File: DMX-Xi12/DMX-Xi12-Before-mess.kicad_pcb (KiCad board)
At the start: 2 copper layers, 177.8 x 196.8 mm, 190 parts, among them Con1 Cortex-10-SWD, Con10 Screw-terminal, Con11 BARREL_JACK, Con2 Screw-terminal, Con3 Screw-terminal, Con4 Screw-terminal, Con5 Screw-terminal, Con6 Screw-terminal, Con7 Screw-terminal, Con8 Screw-terminal, Con9 Screw-terminal, J1 RJ45, J2 RJ45, P3 USB_B, SW1 Switch_SPDT_x2, SW2 DIPS_04, SW3 SW_PUSH, SW4 SW_PUSH, U1 MAX13450E, U10 BTA20, U11 BTA20, U12 BTA20, U13 BTA20, U14 AN-3003, U15 AN-3003, U16 AN-3003, U17 AN-3003, U18 BTA20, U19 BTA20, U2 LPC11U68JBD100E, U20 BTA20, U21 BTA20, U22 AN-3003, U23 AN-3003, U24 AN-3003, U25 AN-3003, U26 BTA20, U27 BTA20, U28 BTA20, U29 BTA20, U3 LTV-354T*, U30 AN-3003, U31 AN-3003, U32 AN-3003, U33 AN-3003, U34 BTA20, U35 BTA20, U36 BTA20, U37 BTA20, U38 AN-3003, U39 AN-3003, U4 7805n, U40 AN-3003, U41 AN-3003, U42 BTA20, U43 BTA20, U44 BTA20, U45 BTA20, U46 AN-3003, U47 AN-3003, U48 AN-3003, U49 AN-3003, U5 LTV-354T*, U50 BTA20, U51 BTA20, U52 BTA20, U53 BTA20, U54 AN-3003, U55 AN-3003, U56 AN-3003, U57 AN-3003, U58 BTA20, U59 BTA20, U6 AN-3003, U60 BTA20, U61 BTA20, U62 AN-3003, U63 AN-3003, U64 AN-3003, U65 AN-3003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

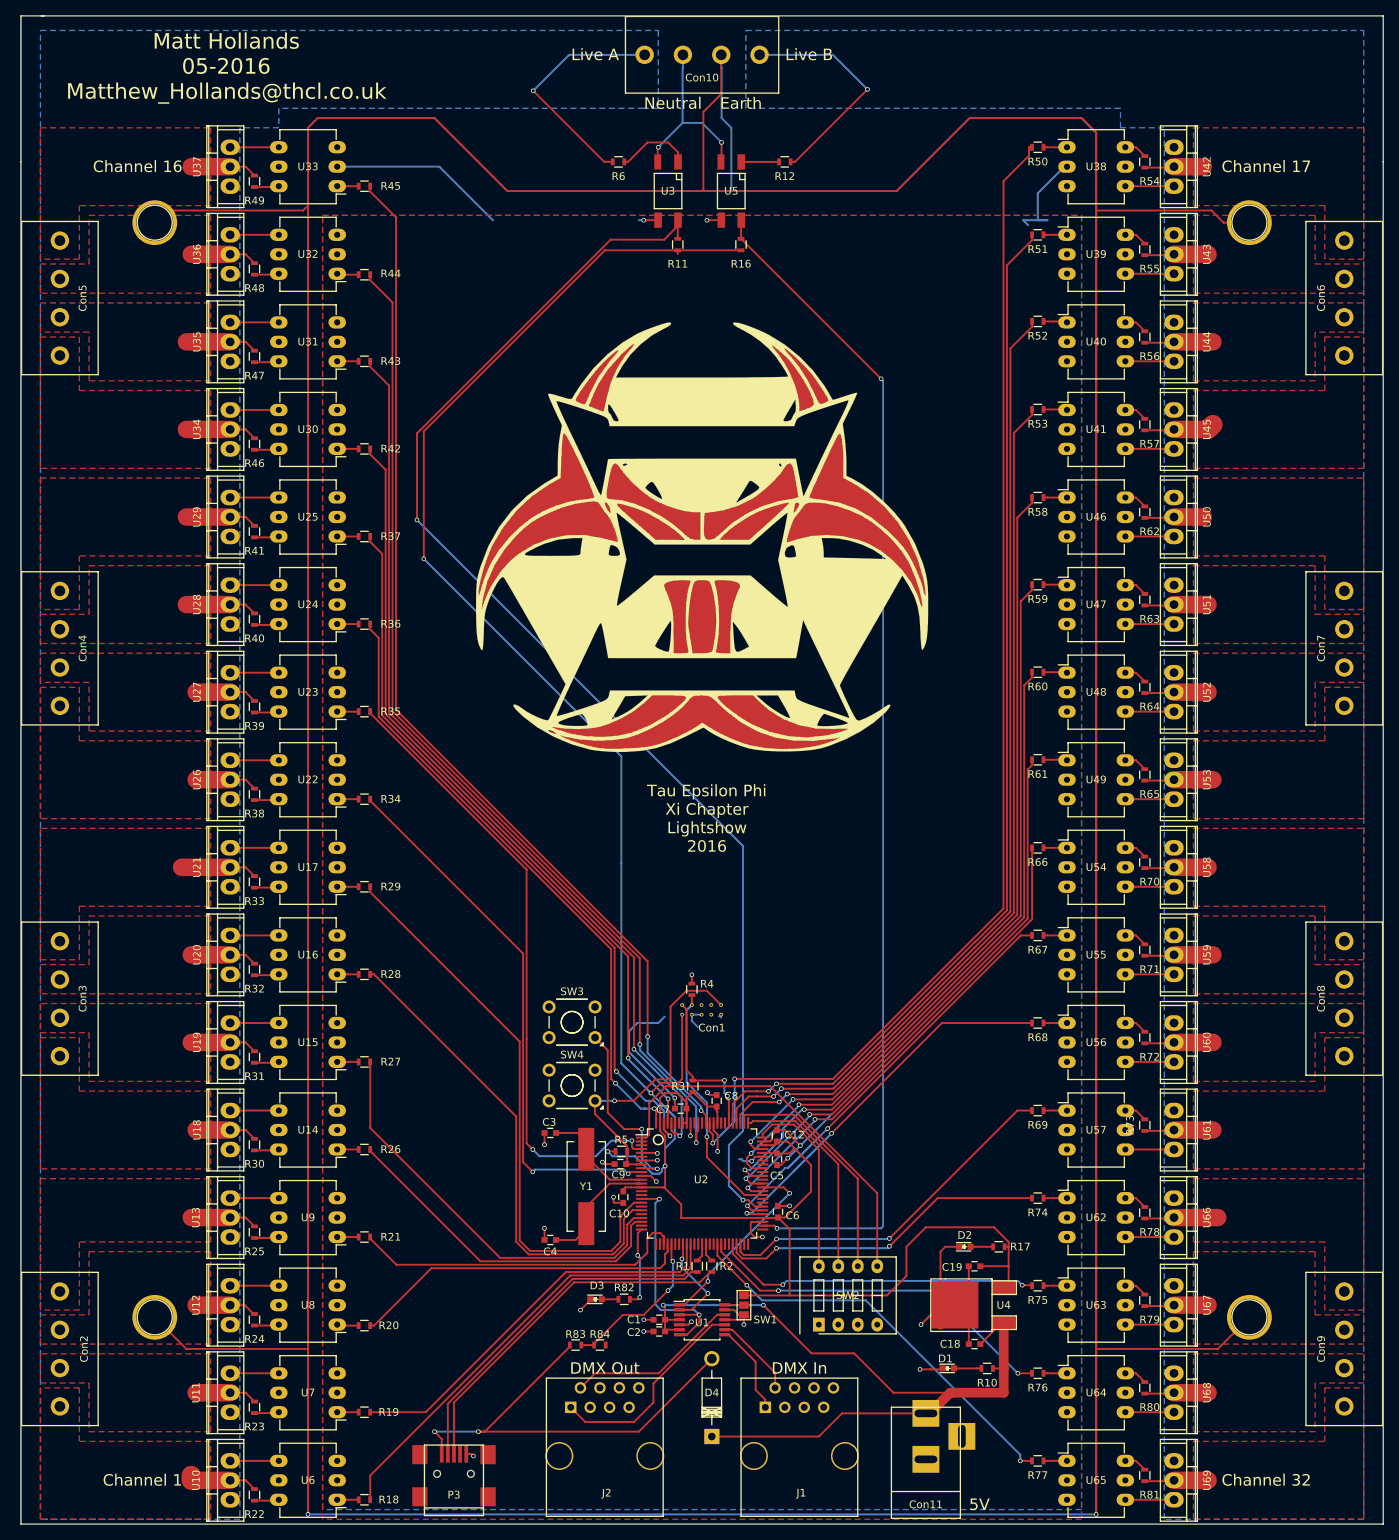
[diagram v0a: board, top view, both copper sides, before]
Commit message: completed board. Schematic, is correct but some part values and numbers need updating! Do not trust the schematic yet
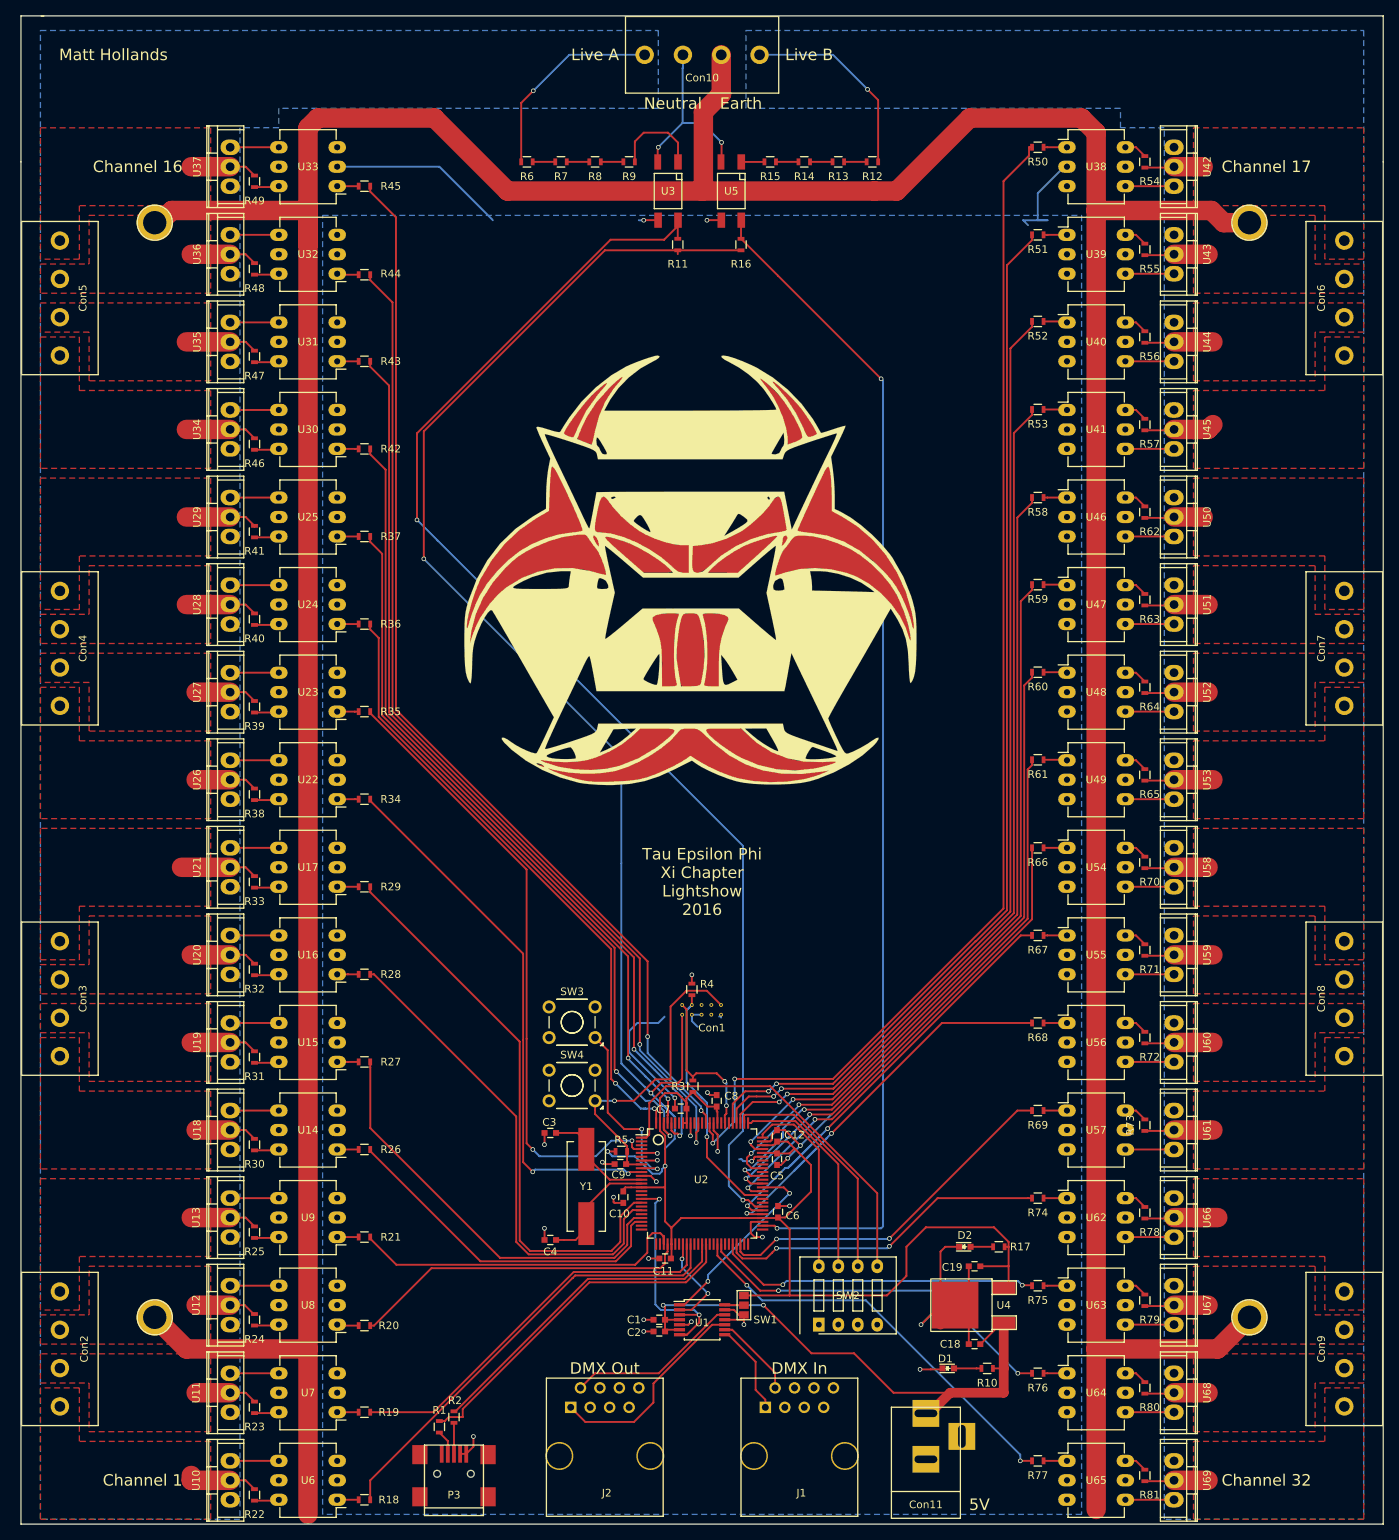
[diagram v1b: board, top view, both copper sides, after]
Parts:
- removed D3: LED, LEDs:LED_0603
- removed D4: D, Diodes_ThroughHole:Diode_DO-41_SOD81_Horizontal_RM10
- removed R82: 330R, Resistors_SMD:R_0603
- removed R83, R84: 10k, Resistors_SMD:R_0603
- added C11: 0.01u, Capacitors_SMD:C_0603, F.Cu at (147.6, 203.5)
- added R13: 2k2, Resistors_SMD:R_0603, F.Cu at (170.2, 60.3)
- added R14: 2k2, Resistors_SMD:R_0603, F.Cu at (165.7, 60.3)
- added R15: 2k2, Resistors_SMD:R_0603, F.Cu at (161.3, 60.3)
- added R7: 2k2, Resistors_SMD:R_0603, F.Cu at (134.0, 60.3)
- added R8: 2k2, Resistors_SMD:R_0603, F.Cu at (138.4, 60.3)
- added R9: 2k2, Resistors_SMD:R_0603, F.Cu at (142.9, 60.3)
- C12: value 0.01u -> 0.1u
- C9: value 1nF -> 4.7uF
- R12, R6: value 100k -> 2k2
- moved R1 39.6 mm to (118.1, 225.4)
- moved R2 39.0 mm to (120.0, 224.2)
- moved R6 12.0 mm to (129.5, 60.3)
- moved R12 11.4 mm to (174.6, 60.3)
- moved G*** 4.58 mm to (150.9, 113.5) (x3)
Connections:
- P3 pad 4: Net-(P3-Pad4) -> GND
- U2 pad 30: Net-(R83-Pad2) -> +3V3
- U2 pad 38: Net-(R1-Pad2) -> Net-(R2-Pad2)
- U2 pad 39: Net-(R2-Pad2) -> Net-(R1-Pad2)
- U2 pad 81: Net-(Con1-Pad2) -> Net-(U2-Pad81)
- U2 pad 82: Net-(U2-Pad82) -> Net-(Con1-Pad2)
- U3 pad 1: Net-(R6-Pad2) -> Net-(R9-Pad2)
- U5 pad 1: Net-(R12-Pad2) -> Net-(R15-Pad2)
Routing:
- net /Earth: track 1177.0 -> 581.7 mm, vias 2 -> 0
- net Net-(P3-Pad1): track 60.2 -> 0.00 mm, vias 2 -> 0
- net Net-(R1-Pad2): track 2.76 -> 46.5 mm
- net Net-(P3-Pad3): track 47.4 -> 4.06 mm
- net Net-(P3-Pad2): track 46.2 -> 3.24 mm
- net Net-(R2-Pad2): track 2.51 -> 43.1 mm
- net +5V: track 108.9 -> 79.7 mm
- net Net-(R83-Pad2): track 20.8 -> 0.00 mm, vias 2 -> 0
- net Net-(R9-Pad2): track 0.00 -> 11.8 mm
- net Net-(U2-Pad25): track 10.6 -> 0.00 mm, vias 2 -> 0
- net Net-(R6-Pad2): track 9.85 -> 2.95 mm
- net +3V3: track 324.4 -> 330.9 mm
- net /Output1/LiveA: track 30.7 -> 26.4 mm
- net /Power/LiveB: track 29.9 -> 26.0 mm
- net Net-(R15-Pad2): track 0.00 -> 3.03 mm
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- removed copper zone on F.Cu, net GND
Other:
- rule pad_to_mask_clearance: 0.0762 -> 0.2
- board text added: "Matt Hollands"
- board text removed: "Matt Hollands 05-2016 Matthew_Hollands@thcl.co.uk"
- board text removed: "dlaw@dlaw.me"
